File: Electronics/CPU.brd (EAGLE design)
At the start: 50 x 50 mm, 12 parts

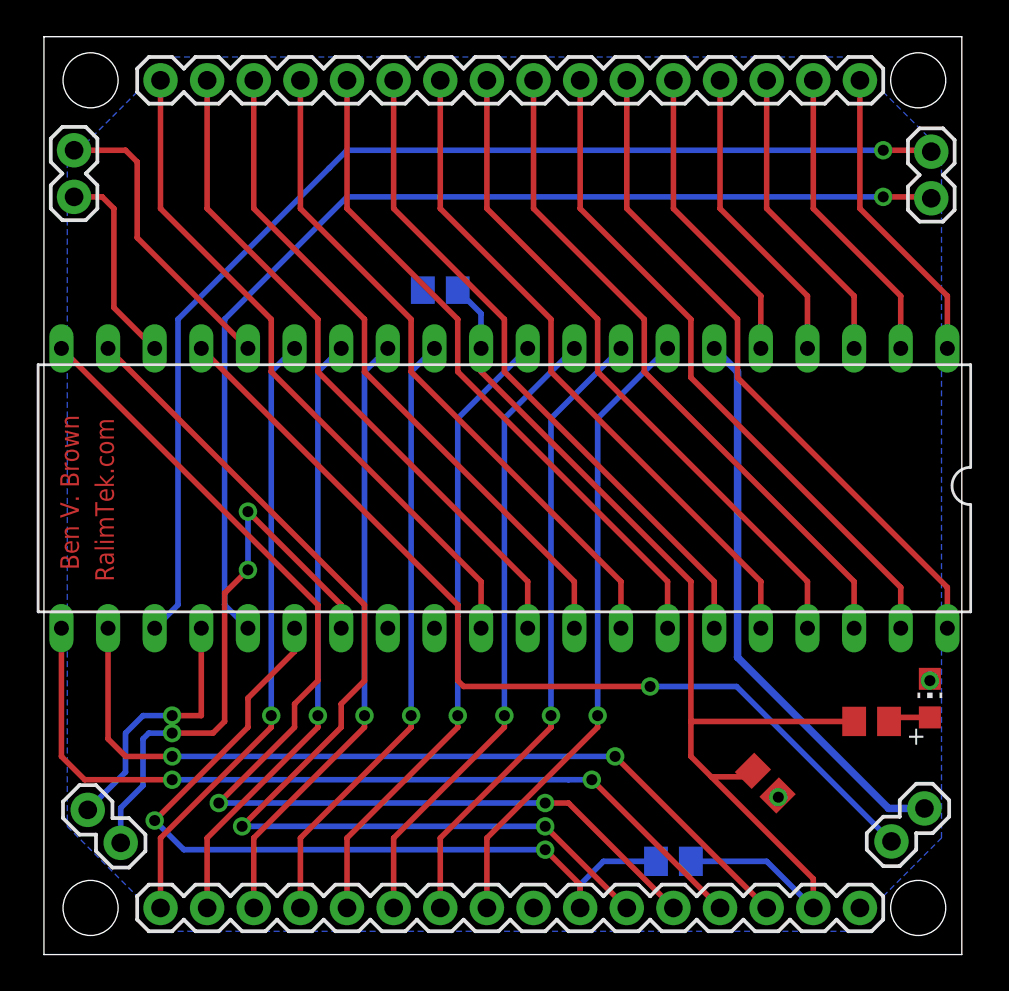
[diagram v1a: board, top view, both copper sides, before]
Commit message: Update board outlines
Adding white line around boards for de-panelization
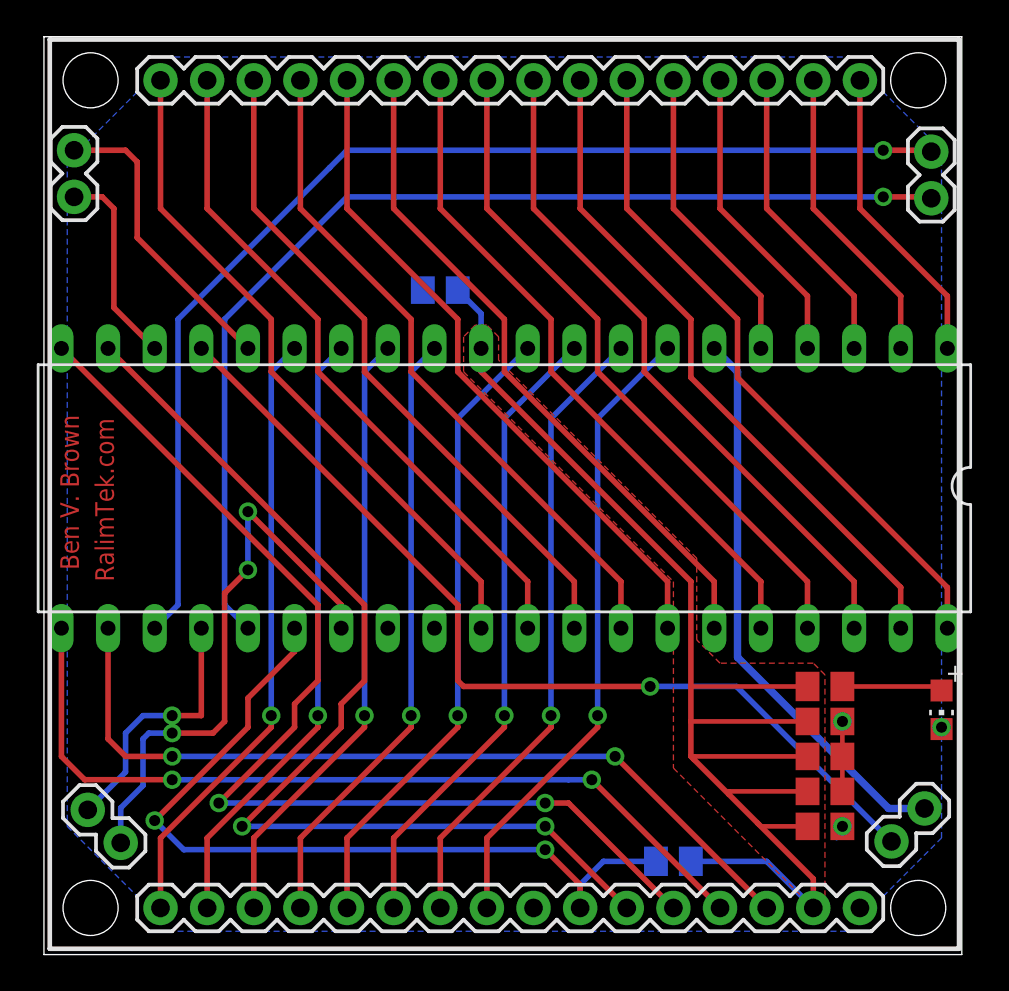
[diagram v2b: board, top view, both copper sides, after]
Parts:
- added C3, C4, C5: 1uF, rcl:C0805
- R2: value (none) -> 10k
- moved C2 4.01 mm to (42.5, 6.99), turned to 0 degrees
- moved R2 3.18 mm to (42.5, 14.6)
- moved LED1 0.90 mm to (48.9, 13.3), turned to 180 degrees
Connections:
- net GND: now also C3.2, C4.2, C5.2
- net VCC: now also C3.1, C4.1, C5.1
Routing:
- net VCC: track 60.7 -> 75.7 mm
- net GND: track 0.35 -> 4.62 mm, vias 2 -> 3
- net N$1: track 2.32 -> 5.49 mm
- added copper zone on layer 1, net VCC
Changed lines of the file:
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@@
 <text x="1.905" y="20.955" size="1.016" layer="1" rot="R90">Ben V. Brown</text>
 <text x="3.81" y="20.32" size="1.016" layer="1" rot="R90">RalimTek.com</text>
+<wire x1="49.8475" y1="49.8475" x2="0.3175" y2="49.8475" width="0.254" layer="21"/>
+<wire x1="0.3175" y1="49.8475" x2="0.3175" y2="0.3175" width="0.254" layer="21"/>
+<wire x1="0.3175" y1="0.3175" x2="49.8475" y2="0.3175" width="0.254" layer="21"/>
+<wire x1="49.8475" y1="0.3175" x2="49.8475" y2="49.8475" width="0.254" layer="21"/>
 </plain>
 <attributes>
@@
 <element name="C1" library="rcl" package="C0805" value="1uF" x="21.59" y="36.195" smashed="yes" rot="MR0"/>
 <element name="R1" library="rcl" package="M0805" value="10K" x="34.29" y="5.08" smashed="yes" rot="MR180"/>
-<element name="C2" library="rcl" package="C0805" value="1uF" x="39.292959375" y="9.339015625" smashed="yes" rot="R315"/>
-<element name="R2" library="rcl" package="M0805" value="" x="45.085" y="12.7" smashed="yes">
-<attribute name="VALUE" x="43.815" y="10.16" size="1.27" layer="27"/>
+<element name="C2" library="rcl" package="C0805" value="1uF" x="42.545" y="6.985" smashed="yes"/>
+<element name="R2" library="rcl" package="M0805" value="10k" x="42.545" y="14.605" smashed="yes"/>
+<element name="LED1" library="adafruit" package="CHIP-LED0805" value="" x="48.895" y="13.335" smashed="yes" rot="R180">
+<attribute name="VALUE" x="46.355" y="14.605" size="1.27" layer="27" rot="R270"/>
 </element>
-<element name="LED1" library="adafruit" package="CHIP-LED0805" value="" x="48.26" y="13.97" smashed="yes">
-<attribute name="VALUE" x="50.8" y="12.7" size="1.27" layer="27" rot="R90"/>
-</element>
+<element name="C3" library="rcl" package="C0805" value="1uF" x="42.545" y="10.795" smashed="yes"/>
+<element name="C4" library="rcl" package="C0805" value="1uF" x="42.545" y="12.7" smashed="yes"/>
+<element name="C5" library="rcl" package="C0805" value="1uF" x="42.545" y="8.89" smashed="yes"/>
 </elements>
 <signals>
@@
 <wire x1="34.29" y1="40.64" x2="34.29" y2="47.625" width="0.3048" layer="1"/>
 </signal>
-<signal name="VCC" airwireshidden="yes">
+<signal name="VCC">
 <contactref element="JP2" pad="15"/>
 <contactref element="IC1" pad="11"/>
 <wire x1="23.8125" y1="33.02" x2="23.8125" y2="31.75" width="0.3048" layer="1"/>
 <wire x1="23.8125" y1="31.75" x2="35.2425" y2="20.32" width="0.3048" layer="1"/>
-<wire x1="35.2425" y1="20.32" x2="35.2425" y2="12.7" width="0.3048" layer="1"/>
+<wire x1="35.2425" y1="20.32" x2="35.2425" y2="14.605" width="0.3048" layer="1"/>
 <contactref element="R1" pad="2"/>
 <contactref element="C1" pad="1"/>
+<wire x1="35.2425" y1="14.605" x2="35.2425" y2="12.7" width="0.3048" layer="1"/>
 <wire x1="35.2425" y1="12.7" x2="35.2425" y2="10.795" width="0.3048" layer="1"/>
 <wire x1="22.54" y1="36.195" x2="23.8125" y2="34.9225" width="0.3048" layer="16"/>
@@
 <contactref element="C2" pad="1"/>
 <wire x1="41.91" y1="2.54" x2="41.91" y2="4.1275" width="0.3048" layer="1"/>
-<wire x1="41.91" y1="4.1275" x2="36.35375" y2="9.68375" width="0.3048" layer="1"/>
-<wire x1="36.35375" y1="9.68375" x2="35.2425" y2="10.795" width="0.3048" layer="1"/>
-<wire x1="38.62120625" y1="10.010765625" x2="38.294190625" y2="9.68375" width="0.3048" layer="1"/>
-<wire x1="38.294190625" y1="9.68375" x2="36.35375" y2="9.68375" width="0.3048" layer="1"/>
+<wire x1="41.91" y1="4.1275" x2="38.89375" y2="7.14375" width="0.3048" layer="1"/>
 <contactref element="R2" pad="1"/>
-<wire x1="44.135" y1="12.7" x2="35.2425" y2="12.7" width="0.3048" layer="1"/>
+<contactref element="C3" pad="1"/>
+<contactref element="C4" pad="1"/>
+<contactref element="C5" pad="1"/>
+<wire x1="38.89375" y1="7.14375" x2="37.30625" y2="8.73125" width="0.3048" layer="1"/>
+<wire x1="37.30625" y1="8.73125" x2="35.40125" y2="10.63625" width="0.3048" layer="1"/>
+<wire x1="35.40125" y1="10.63625" x2="35.2425" y2="10.795" width="0.3048" layer="1"/>
+<wire x1="41.595" y1="14.605" x2="35.2425" y2="14.605" width="0.254" layer="1"/>
+<wire x1="41.595" y1="12.7" x2="35.2425" y2="12.7" width="0.254" layer="1"/>
+<wire x1="41.595" y1="10.795" x2="35.40125" y2="10.795" width="0.254" layer="1"/>
+<wire x1="35.40125" y1="10.795" x2="35.40125" y2="10.63625" width="0.254" layer="1"/>
+<wire x1="41.595" y1="8.89" x2="37.30625" y2="8.89" width="0.254" layer="1"/>
+<wire x1="37.30625" y1="8.89" x2="37.30625" y2="8.73125" width="0.254" layer="1"/>
+<wire x1="41.595" y1="6.985" x2="39.0525" y2="6.985" width="0.254" layer="1"/>
+<wire x1="39.0525" y1="6.985" x2="38.89375" y2="7.14375" width="0.254" layer="1"/>
+<polygon width="0.254" layer="1">
+<vertex x="41.91" y="2.54"/>
+<vertex x="42.545" y="3.175"/>
+<vertex x="42.545" y="15.24"/>
+<vertex x="41.91" y="15.875"/>
+<vertex x="36.83" y="15.875"/>
+<vertex x="35.56" y="17.145"/>
+<vertex x="35.56" y="21.59"/>
+<vertex x="24.765" y="32.385"/>
+<vertex x="24.765" y="33.655"/>
+<vertex x="24.13" y="34.29"/>
+<vertex x="23.495" y="34.29"/>
+<vertex x="22.86" y="33.655"/>
+<vertex x="22.86" y="31.75"/>
+<vertex x="34.29" y="20.32"/>
+<vertex x="34.29" y="10.16"/>
+</polygon>
 </signal>
 <signal name="GND">
@@
 <contactref element="C1" pad="2"/>
 <contactref element="C2" pad="2"/>
-<wire x1="39.964709375" y1="8.6672625" x2="40.005" y2="8.626971875" width="0.3048" layer="1"/>
-<wire x1="40.005" y1="8.626971875" x2="40.005" y2="8.5725" width="0.3048" layer="1"/>
-<via x="40.005" y="8.5725" extent="1-16" drill="0.6" shape="octagon"/>
 <contactref element="LED1" pad="C"/>
-<wire x1="48.26" y1="15.02" x2="48.1625" y2="14.9225" width="0.3048" layer="1"/>
-<wire x1="48.1625" y1="14.9225" x2="48.26" y2="14.9225" width="0.3048" layer="1"/>
-<via x="48.26" y="14.9225" extent="1-16" drill="0.6" shape="octagon"/>
+<contactref element="C3" pad="2"/>
+<contactref element="C4" pad="2"/>
+<contactref element="C5" pad="2"/>
+<wire x1="43.495" y1="6.985" x2="43.4975" y2="6.985" width="0.254" layer="1"/>
+<via x="43.4975" y="6.985" extent="1-16" drill="0.6" shape="octagon"/>
+<wire x1="43.4975" y1="6.985" x2="43.18" y2="6.35" width="0.254" layer="16"/>
+<wire x1="43.18" y1="6.35" x2="43.18" y2="6.6675" width="0.254" layer="16"/>
+<wire x1="43.495" y1="12.7" x2="43.4975" y2="12.7" width="0.254" layer="1"/>
+<via x="43.4975" y="12.7" extent="1-16" drill="0.6" shape="octagon"/>
+<wire x1="43.495" y1="10.795" x2="43.495" y2="12.7" width="0.254" layer="1"/>
+<wire x1="48.895" y1="12.285" x2="48.895" y2="12.3825" width="0.254" layer="1"/>
+<via x="48.895" y="12.3825" extent="1-16" drill="0.6" shape="octagon"/>
+<wire x1="48.895" y1="12.3825" x2="48.895" y2="12.065" width="0.254" layer="16"/>
+<wire x1="43.495" y1="8.89" x2="43.495" y2="10.1575" width="0.254" layer="1"/>
+<wire x1="43.495" y1="10.1575" x2="43.4975" y2="10.16" width="0.254" layer="1"/>
+<wire x1="43.495" y1="10.795" x2="43.495" y2="10.1575" width="0" layer="19" extent="1-1"/>
 </signal>
 <signal name="WR">
@@
 <contactref element="R2" pad="2"/>
 <contactref element="LED1" pad="A"/>
-<wire x1="46.035" y1="12.7" x2="46.255" y2="12.92" width="0.3048" layer="1"/>
-<wire x1="46.255" y1="12.92" x2="48.26" y2="12.92" width="0.3048" layer="1"/>
+<wire x1="43.495" y1="14.605" x2="48.675" y2="14.605" width="0.254" layer="1"/>
+<wire x1="48.675" y1="14.605" x2="48.895" y2="14.385" width="0.254" layer="1"/>
 </signal>
 </signals>

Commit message: Route DIO Breakout + update Text
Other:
- board text added: "Project: Zeta"
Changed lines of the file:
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@@
 <hole x="47.625" y="2.54" drill="3"/>
 <hole x="2.54" y="2.54" drill="3"/>
-<text x="1.905" y="20.955" size="1.016" layer="1" rot="R90">Ben V. Brown</text>
-<text x="3.81" y="20.32" size="1.016" layer="1" rot="R90">RalimTek.com</text>
+<text x="1.905" y="19.685" size="1.016" layer="1" font="vector" rot="R90">Ben V. Brown</text>
+<text x="3.81" y="19.685" size="1.016" layer="1" font="vector" rot="R90">RalimTek.com</text>
 <wire x1="49.8475" y1="49.8475" x2="0.3175" y2="49.8475" width="0.254" layer="21"/>
 <wire x1="0.3175" y1="49.8475" x2="0.3175" y2="0.3175" width="0.254" layer="21"/>
 <wire x1="0.3175" y1="0.3175" x2="49.8475" y2="0.3175" width="0.254" layer="21"/>
 <wire x1="49.8475" y1="0.3175" x2="49.8475" y2="49.8475" width="0.254" layer="21"/>
+<text x="41.275" y="29.845" size="0.8128" layer="21" font="vector">Project: Zeta</text>
 </plain>
 <attributes>

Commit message: Gerbers!
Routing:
- net WAIT: track 14.3 -> 12.5 mm
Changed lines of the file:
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@@
 </class>
 </classes>
-<designrules name="default">
-<description language="de">&lt;b&gt;EAGLE Design Rules&lt;/b&gt;
-&lt;p&gt;
-Die Standard-Design-Rules sind so gewählt, dass sie für
-die meisten Anwendungen passen. Sollte ihre Platine
-besondere Anforderungen haben, treffen Sie die erforderlichen
-Einstellungen hier und speichern die Design Rules unter
-einem neuen Namen ab.</description>
-<description language="en">&lt;b&gt;EAGLE Design Rules&lt;/b&gt;
-&lt;p&gt;
-The default Design Rules have been set to cover
-a wide range of applications. Your particular design
-may have different requirements, so please make the
-necessary adjustments and save your customized
-design rules under a new name.</description>
+<designrules name="dirt_cheap_dirty_boards.v1">
+<description language="en">&lt;b&gt;Dirty Cheap Dirty Board Design Rules&lt;/b&gt;
+&lt;br&gt;
+&lt;br&gt;Min width/Spacing: 5/5mil
+&lt;br&gt;Min diameter of finished hole 12mil</description>
 <param name="layerSetup" value="(1*16)"/>
-<param name="mtCopper" value="0.035mm 0.035mm 0.035mm 0.035mm 0.035mm 0.035mm 0.035mm 0.035mm 0.035mm 0.035mm 0.035mm 0.035mm 0.035mm 0.035mm 0.035mm 0.035mm"/>
-<param name="mtIsolate" value="1.5mm 0.15mm 0.2mm 0.15mm 0.2mm 0.15mm 0.2mm 0.15mm 0.2mm 0.15mm 0.2mm 0.15mm 0.2mm 0.15mm 0.2mm"/>
-<param name="mdWireWire" value="8mil"/>
-<param name="mdWirePad" value="8mil"/>
-<param name="mdWireVia" value="8mil"/>
-<param name="mdPadPad" value="8mil"/>
-<param name="mdPadVia" value="8mil"/>
-<param name="mdViaVia" value="8mil"/>
-<param name="mdSmdPad" value="8mil"/>
-<param name="mdSmdVia" value="8mil"/>
-<param name="mdSmdSmd" value="8mil"/>
+<param name="mtCopper" value="0.035mm 0.0175mm 0.035mm 0.035mm 0.035mm 0.035mm 0.035mm 0.035mm 0.035mm 0.035mm 0.035mm 0.035mm 0.035mm 0.035mm 0.0175mm 0.035mm"/>
+<param name="mtIsolate" value="1.5mm 1.1mm 0.2mm 0.15mm 0.2mm 0.15mm 0.2mm 0.15mm 0.2mm 0.15mm 0.2mm 0.15mm 0.2mm 0.15mm 0.2mm"/>
+<param name="mdWireWire" value="5mil"/>
+<param name="mdWirePad" value="5mil"/>
+<param name="mdWireVia" value="5mil"/>
+<param name="mdPadPad" value="5mil"/>
+<param name="mdPadVia" value="5mil"/>
+<param name="mdViaVia" value="5mil"/>
+<param name="mdSmdPad" value="0mil"/>
+<param name="mdSmdVia" value="0mil"/>
+<param name="mdSmdSmd" value="0mil"/>
 <param name="mdViaViaSameLayer" value="8mil"/>
 <param name="mnLayersViaInSmd" value="2"/>
-<param name="mdCopperDimension" value="40mil"/>
-<param name="mdDrill" value="8mil"/>
+<param name="mdCopperDimension" value="10mil"/>
+<param name="mdDrill" value="10mil"/>
 <param name="mdSmdStop" value="0mil"/>
-<param name="msWidth" value="10mil"/>
-<param name="msDrill" value="24mil"/>
-<param name="msMicroVia" value="9.99mm"/>
+<param name="msWidth" value="5mil"/>
+<param name="msDrill" value="12mil"/>
+<param name="msMicroVia" value="12mil"/>
 <param name="msBlindViaRatio" value="0.5"/>
 <param name="rvPadTop" value="0.25"/>
@@
 <param name="rlMinPadBottom" value="10mil"/>
 <param name="rlMaxPadBottom" value="20mil"/>
-<param name="rlMinViaOuter" value="8mil"/>
+<param name="rlMinViaOuter" value="6mil"/>
 <param name="rlMaxViaOuter" value="20mil"/>
-<param name="rlMinViaInner" value="8mil"/>
+<param name="rlMinViaInner" value="6mil"/>
 <param name="rlMaxViaInner" value="20mil"/>
 <param name="rlMinMicroViaOuter" value="4mil"/>
@@
 <param name="psTop" value="-1"/>
 <param name="psBottom" value="-1"/>
-<param name="psFirst" value="-1"/>
+<param name="psFirst" value="0"/>
 <param name="psElongationLong" value="100"/>
 <param name="psElongationOffset" value="100"/>
 <param name="mvStopFrame" value="1"/>
 <param name="mvCreamFrame" value="0"/>
-<param name="mlMinStopFrame" value="4mil"/>
-<param name="mlMaxStopFrame" value="4mil"/>
+<param name="mlMinStopFrame" value="2mil"/>
+<param name="mlMaxStopFrame" value="2mil"/>
 <param name="mlMinCreamFrame" value="0mil"/>
 <param name="mlMaxCreamFrame" value="0mil"/>
-<param name="mlViaStopLimit" value="0mil"/>
+<param name="mlViaStopLimit" value="25mil"/>
 <param name="srRoundness" value="0"/>
 <param name="srMinRoundness" value="0mil"/>
@@
 <param name="checkAngle" value="0"/>
 <param name="checkFont" value="1"/>
-<param name="checkRestrict" value="1"/>
+<param name="checkRestrict" value="0"/>
 <param name="useDiameter" value="13"/>
 <param name="maxErrors" value="50"/>
@@
 <signal name="WAIT">
 <contactref element="IC1" pad="24"/>
-<wire x1="8.5725" y1="17.78" x2="8.5725" y2="13.0175" width="0.3048" layer="1"/>
+<wire x1="8.5725" y1="17.78" x2="8.5725" y2="16.1925" width="0.3048" layer="1"/>
 <contactref element="JP3" pad="2"/>
-<wire x1="8.5725" y1="13.0175" x2="6.985" y2="13.0175" width="0.3048" layer="1"/>
-<via x="6.985" y="13.0175" extent="1-16" drill="0.6" shape="octagon"/>
-<wire x1="6.985" y1="13.0175" x2="5.3975" y2="13.0175" width="0.3048" layer="16"/>
-<wire x1="5.3975" y1="13.0175" x2="4.445" y2="12.065" width="0.3048" layer="16"/>
 <wire x1="4.445" y1="12.065" x2="4.445" y2="9.94210625" width="0.3048" layer="16"/>
 <wire x1="4.445" y1="9.94210625" x2="2.38591875" y2="7.883025" width="0.3048" layer="16"/>
+<wire x1="4.445" y1="12.065" x2="6.985" y2="14.605" width="0.3048" layer="16"/>
+<via x="6.985" y="14.605" extent="1-16" drill="0.6" shape="octagon"/>
+<wire x1="6.985" y1="14.605" x2="8.5725" y2="16.1925" width="0.3048" layer="1"/>
 </signal>
 <signal name="NMI">
